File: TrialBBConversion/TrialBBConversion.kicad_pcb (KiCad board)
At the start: 2 copper layers, 38 parts, among them SW1 SW_SPDT, SW2 SW_Push, SW3 SW_Push, U1 DRV883-MPV_Symbol_Lib, U2 Color_Sensor-MPV_Symbol_Lib, U3 a-24543.5mmAudio, U4 SPX3819M5-L-3-3, X1 Arduino_Pro_Mini

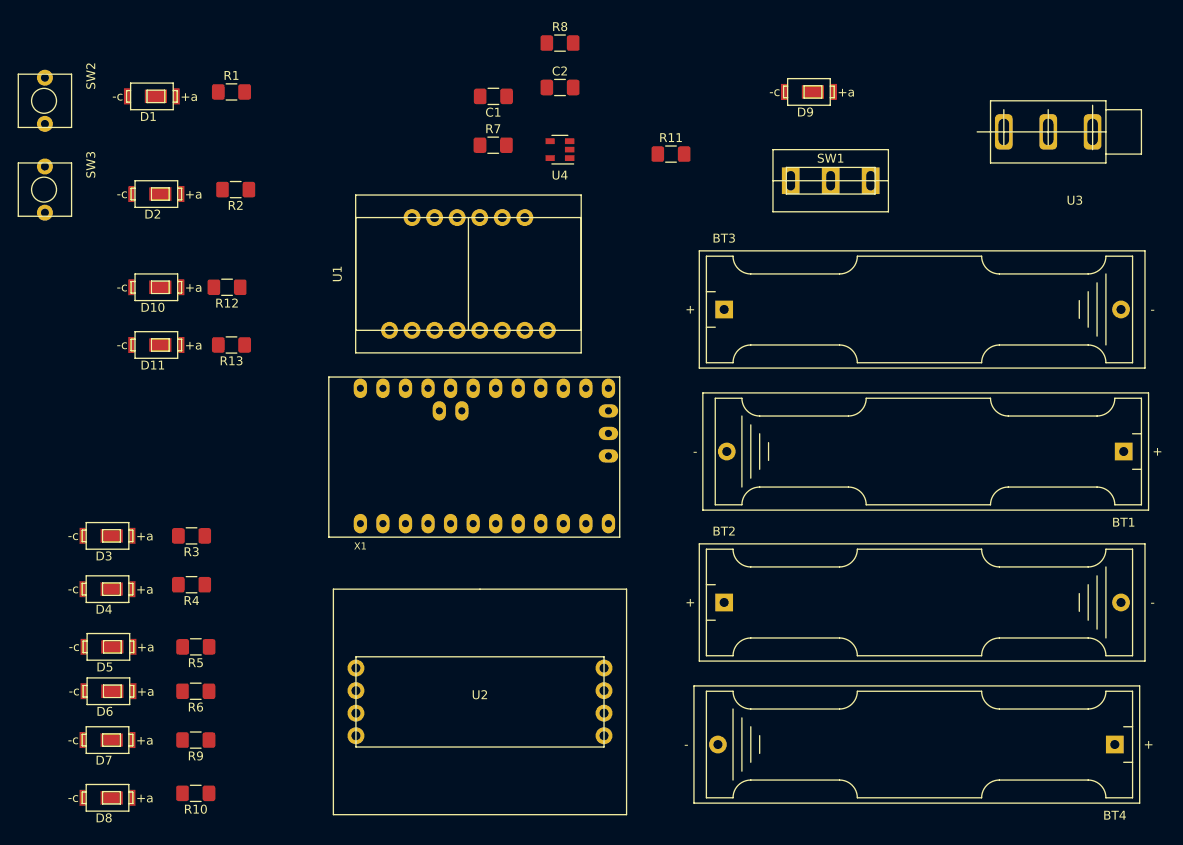
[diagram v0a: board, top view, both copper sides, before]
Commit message: updated routing pcb
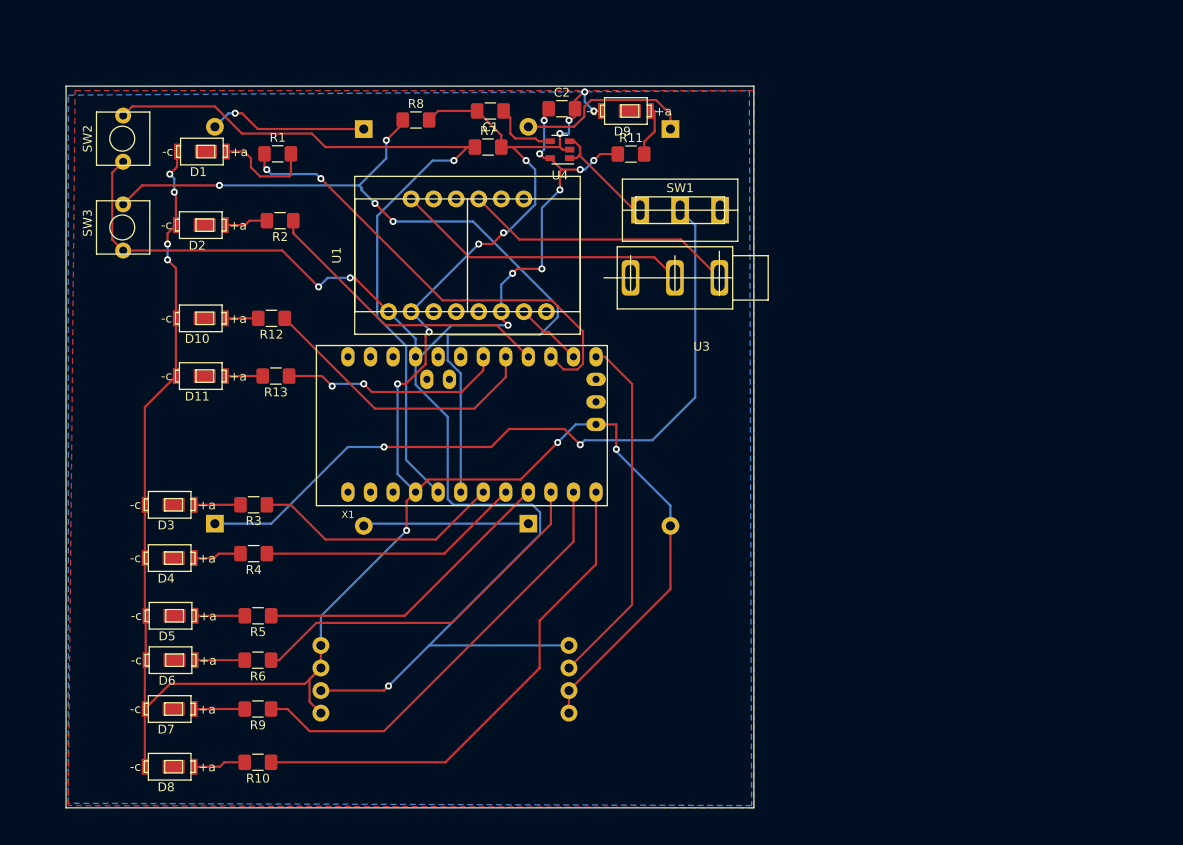
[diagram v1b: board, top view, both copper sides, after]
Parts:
- BT1, BT2, BT3, BT4, U2: moved to B.Cu
- moved BT1 93.0 mm to (152.9, 74.7), turned to 270 degrees
- moved BT4 85.5 mm to (187.5, 74.7), turned to 270 degrees
- moved BT3 62.2 mm to (136.1, 119.1), turned to 90 degrees
- moved U3 45.1 mm to (194.5, 87.9)
- moved BT2 23.8 mm to (171.4, 119.1), turned to 90 degrees
- moved U2 23.2 mm to (162.1, 149.4)
- moved D9 20.7 mm to (185.3, 71.1)
- moved R8 18.4 mm to (158.8, 73.7)
- moved SW1 17.3 mm to (182.0, 87.3)
- moved SW2 9.79 mm to (122.8, 72.8)
- moved SW3 9.79 mm to (122.8, 82.8)
- moved R1 8.70 mm to (143.2, 77.5)
- moved D1 8.39 mm to (137.5, 75.7)
- moved D3 7.83 mm to (133.9, 115.5)
- moved D4 7.83 mm to (133.9, 121.5)
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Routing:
- net GND: track 0.00 -> 272.1 mm, vias 0 -> 16
- net 3.3vlabel: track 0.00 -> 179.7 mm, vias 0 -> 11
- net Net-(R8-Pad1): track 0.00 -> 97.8 mm, vias 0 -> 4
- net Net-(R7-Pad1): track 0.00 -> 90.1 mm, vias 0 -> 1
- net Net-(BT3-Pad1): track 0.00 -> 83.3 mm, vias 0 -> 2
- net Net-(R10-Pad1): track 0.00 -> 57.1 mm
- net Net-(R1-Pad1): track 0.00 -> 53.2 mm, vias 0 -> 3
- net Net-(R9-Pad1): track 0.00 -> 49.5 mm
- net Net-(R6-Pad1): track 0.00 -> 41.5 mm
- net Net-(U2-Pad6): track 0.00 -> 40.3 mm
- net Net-(R5-Pad1): track 0.00 -> 34.7 mm
- net Net-(R2-Pad1): track 0.00 -> 33.7 mm
- net Net-(U1-Pad14): track 0.00 -> 33.4 mm
- net Net-(R12-Pad1): track 0.00 -> 32.9 mm
- net Net-(U1-Pad11): track 0.00 -> 30.8 mm
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- added copper zone on F.Cu, net 3.3vlabel
- added copper zone on B.Cu, net GND
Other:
- board outline added: 77.5 x 81.3 mm

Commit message: mostly improved silkscreen
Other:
- board text added: "100% 80% 60% 40% 20% 0%"
- board text added: "3.3v Pro Mini 8Mhz"
- board text added: "Blk Cal"
- board text added: "DRV8833 Module"
- board text added: "GND GND 3.3v GND"
- board text added: "Motor"
- board text added: "Power"
- board text added: "Red Cal"
- board text added: "S3 S2 Out GND"
